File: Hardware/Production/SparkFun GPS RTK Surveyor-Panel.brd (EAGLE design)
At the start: 219.3 x 144.2 mm, 588 parts, among them J13 Internal, J16 microSD, J17 Qwiic Right Angle, J19 External, J20 USB Female Type C Connector, J21 Power Switch, J24 Start Base, J25 USB Female Type C Connector, J3 USB Female Type C Connector, J32 microSD, J34 Qwiic Right Angle, J36 Internal, J37 External, J38 USB Female Type C Connector, J39 Power Switch, J4 External, J42 Start Base, J43 USB Female Type C Connector, J5 USB Female Type C Connector, J50 microSD, J52 Qwiic Right Angle, J54 Internal, J6 Start Base, J7 Power Switch, Q1 MBT3904DW1T1, Q2 MBT3904DW1T1, Q3 MBT3904DW1T1, U1 ESP-WROOM-3232D-NARROW, U10 MCP73833, U11 MAX17048, U12 3.3V, U13 MCP73833, U14 ESP-WROOM-3232D-NARROW, U15 3.3V, U16 U-BLOX_ZED-F9P, U17 CH340C, U18 MAX17048, U19 3.3V, U2 3.3V, U20 MCP73833, U21 ESP-WROOM-3232D-NARROW, U3 U-BLOX_ZED-F9P, U4 3.3V, U5 3.3V, U6 CH340C, U7 MAX17048, U8 U-BLOX_ZED-F9P, U9 CH340C

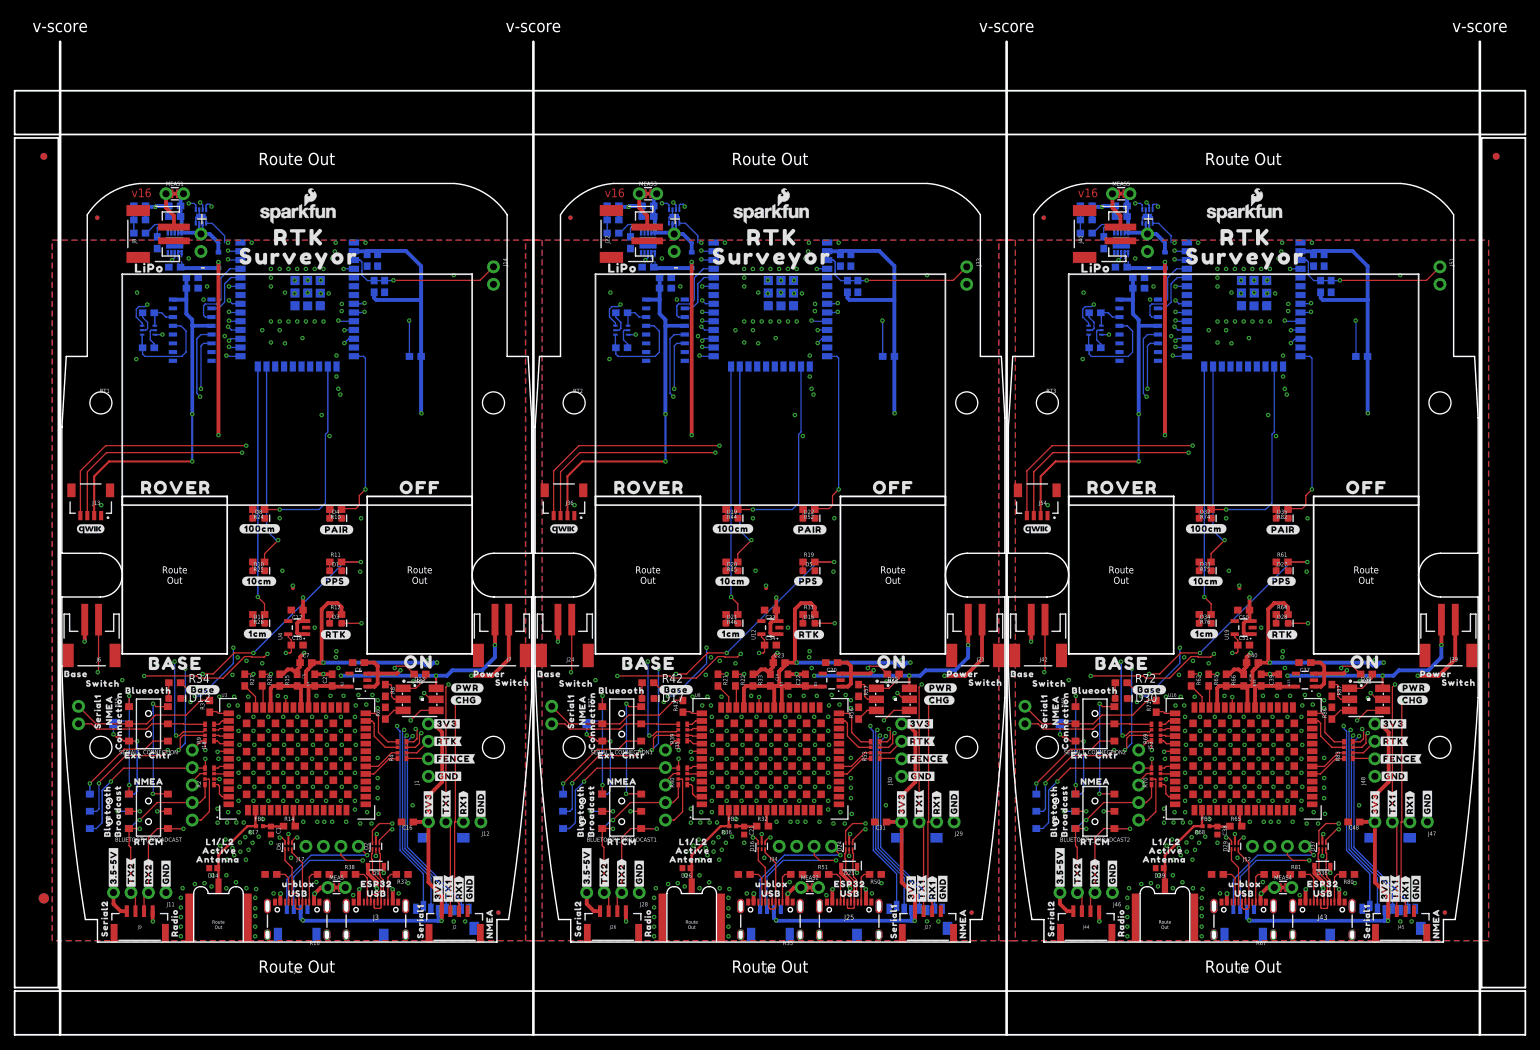
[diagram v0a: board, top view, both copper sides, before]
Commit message: Update panel to v17
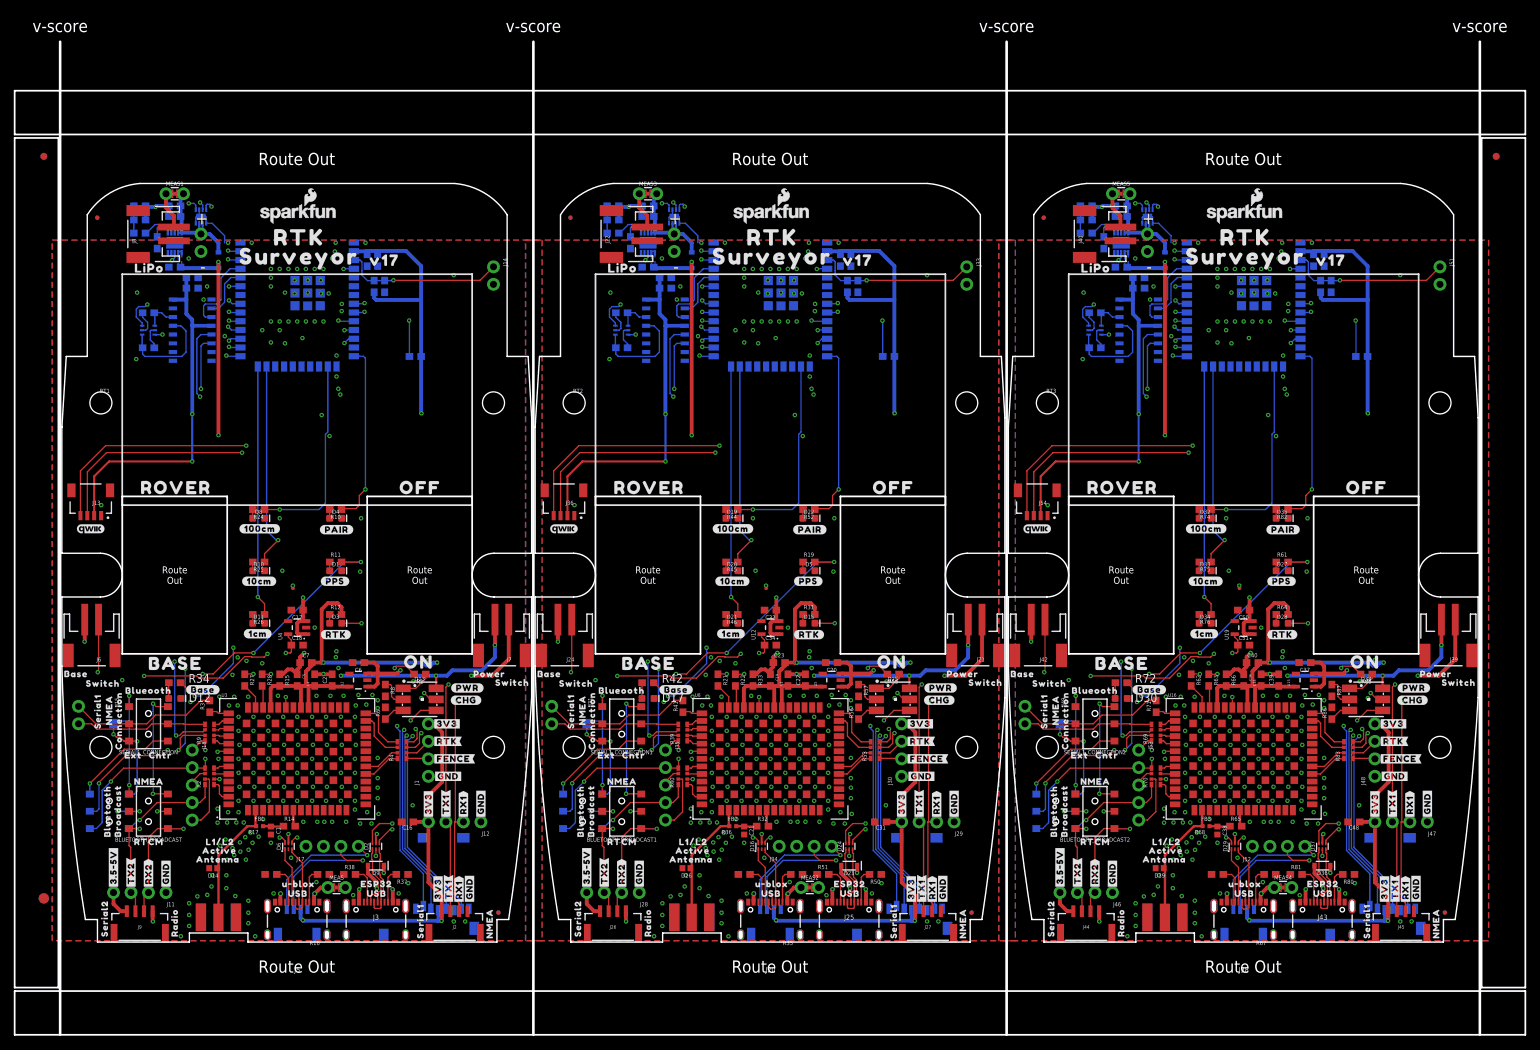
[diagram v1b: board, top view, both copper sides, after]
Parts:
- added U$277: (no value), output:PORT3
- added U$278: (no value), output:PPS#RESET0
- added U$279: (no value), output:NMEA#SERIAL1
- added U$280: (no value), SparkFun-Aesthetics:QWIIC_4MM
- added U$281, U$282: (no value), output:V170
- E1, E2, E3: device SparkFun-RF:SMA-EDGE-SMD -> SparkFun-RF:SMA-EDGE
- U$100: device output:_SURVEYOR3 -> output:#GND#0
- U$101: device output:#RTK#1 -> output:ANTENNA0
- U$102: device output:ACTIVE0 -> output:_SURVEYOR3
- U$103: device output:L1#L21 -> output:#RTK#1
- U$104: device output:#PAIR#0 -> output:ACTIVE0
- U$105: device SparkFun GPS RTK Surveyor:1553DBK-ENCLOSURE -> output:L1#L21
- U$106: device output:#CHG#0 -> output:#PAIR#0
- U$107: device output:LIPO0 -> SparkFun GPS RTK Surveyor:1553DBK-ENCLOSURE
- U$108: device output:U#BLOX0 -> output:#CHG#0
- U$109: device output:USB1 -> output:LIPO0
- U$110: device output:SERIAL20 -> output:U#BLOX0
- U$111: device output:SERIAL10 -> output:USB1
- U$112, U$206: device SparkFun GPS RTK Surveyor:ROCKER_SWITCH -> output:SERIAL20
- U$113: device output:#BASE#0 -> output:SERIAL10
- U$115: device SparkFun GPS RTK Surveyor:LIGHT_PIPE_3MM -> output:#BASE#0
- U$116, U$208: device SparkFun GPS RTK Surveyor:LIGHT_PIPE_3MM -> SparkFun GPS RTK Surveyor:ROCKER_SWITCH
- U$117: device output:BASE2 -> SparkFun GPS RTK Surveyor:LIGHT_PIPE_3MM
- U$118: device output:OFF1 -> SparkFun GPS RTK Surveyor:LIGHT_PIPE_3MM
- U$119: device output:ON0 -> output:BASE2
- U$120: device output:ROVER3 -> output:OFF1
- U$121: device output:#RX2#2 -> output:ON0
- U$122: device output:#TX2#1 -> output:ROVER3
- U$123: device output:#RX1#2 -> output:#RX2#2
- U$124: device output:#TX1#1 -> output:#TX2#1
- U$125: device output:#3V3#0 -> output:#RX1#2
- U$126, U$169: device output:#GND#0 -> output:#TX1#1
- U$127: device output:#GND#0 -> output:#3V3#0
- U$128: device output:NMEA1 -> output:#GND#0
- U$129: device output:RADIO0 -> output:#GND#0
- U$130: device output:##RST##4 -> output:NMEA1
- U$131: device output:##SAFE##5 -> output:RADIO0
- U$132: device output:#FENCE#3 -> output:##RST##4
- U$133: device output:#INT#0 -> output:##SAFE##5
- U$134: device output:BASE0 -> output:#FENCE#3
- U$135, U$229: device output:SWITCH1 -> output:#INT#0
- U$136: device output:POWER0 -> output:BASE0
- U$138: device output:#3#5#5V#0 -> output:POWER0
- U$139, U$231: device output:BLUETOOTH2 -> output:SWITCH1
- U$140: device output:BROADCAST3 -> output:#3#5#5V#0
- U$141: device output:NMEA1 -> output:BLUETOOTH2
- U$142: device output:RTCM0 -> output:BROADCAST3
- U$143: device output:BLUEOOTH3 -> output:NMEA1
- U$144: device output:CNTR1 -> output:RTCM0
- U$145: device output:EXT0 -> output:BLUEOOTH3
- U$146: device output:NMEA2 -> output:CNTR1
- U$147: device output:SERIAL10 -> output:EXT0
- U$148: device output:CONNECTION1 -> output:NMEA2
- U$149, U$207: device SparkFun GPS RTK Surveyor:LIGHT_PIPE_3MM -> output:SERIAL10
- U$150: device output:#PPS#0 -> output:CONNECTION1
- U$151: device output:_SURVEYOR3 -> SparkFun GPS RTK Surveyor:LIGHT_PIPE_3MM
- U$152: device output:#RX#2 -> output:#PPS#0
- U$153: device output:ZED0 -> output:_SURVEYOR3
- U$154: device output:#TX#1 -> output:#RX#2
- U$155: device output:#DUAL#0 -> output:ZED0
- U$156, U$250: device SparkFun GPS RTK Surveyor:LIGHT_PIPE_3MM -> output:#TX#1
- U$157, U$251: device SparkFun GPS RTK Surveyor:LIGHT_PIPE_3MM -> output:#DUAL#0
- U$161, U$253: device output:#1CM#0 -> SparkFun GPS RTK Surveyor:LIGHT_PIPE_3MM
- U$162, U$254: device output:#10CM#1 -> SparkFun GPS RTK Surveyor:LIGHT_PIPE_3MM
- U$163: device output:#100CM#2 -> output:#1CM#0
- U$164: device output:USB1 -> output:#10CM#1
- U$165: device output:ESP320 -> output:#100CM#2
- U$166: device output:#3V3#0 -> output:USB1
- U$167: device output:#TX1#1 -> output:ESP320
- U$168: device output:#RX1#2 -> output:#3V3#0
- U$170: device output:MICROSD0 -> output:#RX1#2
- U$171: device output:#GND#1 -> output:#GND#0
- U$172: device output:#ESP_RST#0 -> output:MICROSD0
- U$173: device output:RTK0 -> output:#GND#1
- U$174: device output:RTK0 -> output:#ESP_RST#0
- U$175: device output:#GND#2 -> output:RTK0
- U$176: device output:#3V3#2 -> output:RTK0
- U$177: device output:#SCL#1 -> output:#GND#2
- U$178: device output:#SDA#0 -> output:#3V3#2
- U$179: device output:#D_SEL#0 -> output:#SCL#1
- U$180: device output:DATA2 -> output:#SDA#0
- U$181: device output:PORT3 -> output:#D_SEL#0
- U$182: device output:PPS#RESET0 -> output:DATA2
- U$183: device output:NMEA#SERIAL1 -> output:PORT3
- U$184: device SparkFun-Aesthetics:QWIIC_4MM -> output:PPS#RESET0
- U$185: device SparkFun-Aesthetics:QWIIC_4MM -> output:NMEA#SERIAL1
- U$186: device output:#RTK#0 -> SparkFun-Aesthetics:QWIIC_4MM
- U$187, U$95: device output:#PPS#1 -> output:V170
- U$188: device output:#PWR#2 -> output:V170
- U$189: device output:#3V3#0 -> SparkFun-Aesthetics:QWIIC_4MM
- U$190: device output:#GND#0 -> output:#RTK#0
- U$191: device output:ANTENNA0 -> output:#PPS#1
- U$192: device output:_SURVEYOR3 -> output:#PWR#2
- U$193: device output:#RTK#1 -> output:#3V3#0
- U$194: device output:ACTIVE0 -> output:#GND#0
- U$195: device output:L1#L21 -> output:ANTENNA0
- U$196: device output:#PAIR#0 -> output:_SURVEYOR3
- U$197: device SparkFun GPS RTK Surveyor:1553DBK-ENCLOSURE -> output:#RTK#1
- U$198: device output:#CHG#0 -> output:ACTIVE0
- U$199: device output:LIPO0 -> output:L1#L21
- U$200: device output:U#BLOX0 -> output:#PAIR#0
- U$201: device output:USB1 -> SparkFun GPS RTK Surveyor:1553DBK-ENCLOSURE
- U$202: device output:SERIAL20 -> output:#CHG#0
- U$203: device output:SERIAL10 -> output:LIPO0
- U$204: device SparkFun GPS RTK Surveyor:ROCKER_SWITCH -> output:U#BLOX0
- U$205: device output:#BASE#0 -> output:USB1
- U$209: device output:BASE2 -> output:#BASE#0
- U$210: device output:OFF1 -> SparkFun GPS RTK Surveyor:ROCKER_SWITCH
- U$211: device output:ON0 -> SparkFun GPS RTK Surveyor:LIGHT_PIPE_3MM
- U$212: device output:ROVER3 -> SparkFun GPS RTK Surveyor:LIGHT_PIPE_3MM
- U$213: device output:#RX2#2 -> output:BASE2
- U$214: device output:#TX2#1 -> output:OFF1
- U$215: device output:#RX1#2 -> output:ON0
- U$216: device output:#TX1#1 -> output:ROVER3
- U$217: device output:#3V3#0 -> output:#RX2#2
- U$218: device output:#GND#0 -> output:#TX2#1
- U$219: device output:#GND#0 -> output:#RX1#2
- U$220: device output:NMEA1 -> output:#TX1#1
- U$221: device output:RADIO0 -> output:#3V3#0
- U$222: device output:##RST##4 -> output:#GND#0
- U$223: device output:##SAFE##5 -> output:#GND#0
- U$224: device output:#FENCE#3 -> output:NMEA1
- U$225: device output:#INT#0 -> output:RADIO0
- U$226: device output:BASE0 -> output:##RST##4
- U$227: device output:SWITCH1 -> output:##SAFE##5
- U$228: device output:POWER0 -> output:#FENCE#3
- U$230: device output:#3#5#5V#0 -> output:BASE0
- U$232: device output:BROADCAST3 -> output:POWER0
- U$233: device output:NMEA1 -> output:SWITCH1
- U$234: device output:RTCM0 -> output:#3#5#5V#0
- U$235: device output:BLUEOOTH3 -> output:BLUETOOTH2
- U$236: device output:CNTR1 -> output:BROADCAST3
- U$237: device output:EXT0 -> output:NMEA1
- U$238: device output:NMEA2 -> output:RTCM0
- U$239: device output:SERIAL10 -> output:BLUEOOTH3
- U$240: device output:CONNECTION1 -> output:CNTR1
- U$241: device SparkFun GPS RTK Surveyor:LIGHT_PIPE_3MM -> output:EXT0
- U$242: device output:#PPS#0 -> output:NMEA2
- U$243: device output:_SURVEYOR3 -> output:SERIAL10
- U$244: device output:#RX#2 -> output:CONNECTION1
- U$245: device output:ZED0 -> SparkFun GPS RTK Surveyor:LIGHT_PIPE_3MM
- U$246: device output:#TX#1 -> output:#PPS#0
- U$247: device output:#DUAL#0 -> output:_SURVEYOR3
- U$248: device SparkFun GPS RTK Surveyor:LIGHT_PIPE_3MM -> output:#RX#2
- U$249: device SparkFun GPS RTK Surveyor:LIGHT_PIPE_3MM -> output:ZED0
- U$255: device output:#100CM#2 -> SparkFun GPS RTK Surveyor:LIGHT_PIPE_3MM
- U$256: device output:USB1 -> SparkFun GPS RTK Surveyor:LIGHT_PIPE_3MM
- U$257: device output:ESP320 -> output:#1CM#0
- U$258: device output:#3V3#0 -> output:#10CM#1
- U$259: device output:#TX1#1 -> output:#100CM#2
- U$260: device output:#RX1#2 -> output:USB1
- U$261: device output:#GND#0 -> output:ESP320
- U$262: device output:MICROSD0 -> output:#3V3#0
- U$263: device output:#GND#1 -> output:#TX1#1
- U$264: device output:#ESP_RST#0 -> output:#RX1#2
- U$265: device output:RTK0 -> output:#GND#0
- U$266: device output:RTK0 -> output:MICROSD0
- U$267: device output:#GND#2 -> output:#GND#1
- U$268: device output:#3V3#2 -> output:#ESP_RST#0
- U$269: device output:#SCL#1 -> output:RTK0
- U$270: device output:#SDA#0 -> output:RTK0
- U$271: device output:#D_SEL#0 -> output:#GND#2
- U$272: device output:DATA2 -> output:#3V3#2
- U$273: device output:PORT3 -> output:#SCL#1
- U$274: device output:PPS#RESET0 -> output:#SDA#0
- U$275: device output:NMEA#SERIAL1 -> output:#D_SEL#0
- U$276: device SparkFun-Aesthetics:QWIIC_4MM -> output:DATA2
- U$94: device output:#RTK#0 -> output:V170
- U$96: device output:#PWR#2 -> output:#RTK#0
- U$97: device output:#3V3#0 -> output:#PPS#1
- U$98: device output:#GND#0 -> output:#PWR#2
- U$99: device output:ANTENNA0 -> output:#3V3#0
- moved U$203 105.6 mm to (150.1, 97.9), turned to 0 degrees
- moved U$186 103.3 mm to (72.9, 60.0)
- moved U$185 97.6 mm to (75.4, 23.7)
- moved U$109 92.9 mm to (81.4, 97.9)
- moved U$188 91.8 mm to (102.9, 48.2), flipped to the bottom
- moved U$265 88.5 mm to (198.2, 17.9), turned to 90 degrees
- moved U$269 86.3 mm to (171.8, 102.3), flipped to the top, turned to 0 degrees
- moved U$175 85.7 mm to (103.1, 102.3), flipped to the top, turned to 0 degrees
- moved U$268 84.9 mm to (199.5, 98.0), turned to 0 degrees
- moved U$199 83.6 mm to (157.6, 14.5)
- moved U$267 83.3 mm to (199.5, 95.4), turned to 0 degrees
- moved U$172 83.2 mm to (130.0, 14.8), turned to 270 degrees
- moved U$94 80.5 mm to (46.9, 99.0)
- moved U$264 80.2 mm to (195.7, 17.9), flipped to the top, turned to 90 degrees
- moved U$263 77.8 mm to (193.2, 17.9), flipped to the top, turned to 90 degrees
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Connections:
- net GND: now also E1.GND@2, E1.GND@3
- net GND1: now also E2.GND@2, E2.GND@3
- net GND2: now also E3.GND@2, E3.GND@3
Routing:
- net GPS_ANT2: track 14.2 -> 18.8 mm
- net GPS_ANT3: track 14.2 -> 18.8 mm
- net GPS_ANT1: track 14.2 -> 18.8 mm
- net GND2: vias 194 -> 189
- net GND1: vias 194 -> 189
- net GND: vias 194 -> 189
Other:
- outline, holes or cut-outs redrawn
- board text removed: "v16"
